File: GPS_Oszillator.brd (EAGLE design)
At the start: 100 x 80 mm, 33 parts, among them IC1 74ACT04D, IC2 7805TV, X1 ST-SMB-V, X2 ST-SMB-V

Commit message: Add files via upload
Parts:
- removed JP1: to_PB6, pinhead:1X02
- moved C12 41.6 mm to (91.7, 10.8), turned to 0 degrees
- moved JP6 6.40 mm to (25.8, 50.4), turned to 0 degrees
- moved C13 4.50 mm to (30.8, 54.8), turned to 90 degrees
- moved R4 3.05 mm to (20.7, 49.4), turned to 0 degrees
- moved IC1 0.45 mm to (19.4, 39.7)
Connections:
- removed net N$1: IC1.2, R3.2
- removed net RESET: U$2.P$4
- new net PPS_IN: IC1.2, R3.2, U$4.34
- new net PWM_OUT: IC1.11, U$4.32
- new net RST: U$2.P$4, U$4.17
- net 10MHZ_IN: now also U$4.35; no longer JP1.1
- net DC: now also U$4.16
- net GND: no longer IC1.11, JP1.2
- net PWM_16BIT: now also IC1.10
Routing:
- net RESET: track 73.5 -> 0.00 mm
- net 5V0: track 114.4 -> 179.6 mm
- net 3V3: track 45.2 -> 101.7 mm, vias 0 -> 2
- net DC: track 74.2 -> 33.3 mm, vias 0 -> 2
- net CS: track 71.8 -> 33.3 mm
- net RST: track 0.00 -> 33.4 mm, vias 0 -> 2
- net PPS_IN: track 0.00 -> 24.4 mm, vias 0 -> 1
- net PWM_OUT: track 0.00 -> 21.3 mm, vias 0 -> 2
- net N$1: track 20.2 -> 0.00 mm, vias 2 -> 0
- net ESP32_EN: track 0.00 -> 8.07 mm
- net 10MHZ_IN: track 38.1 -> 45.0 mm, vias 0 -> 1
- net MOSI: track 55.2 -> 61.3 mm
- net N$4: track 0.00 -> 6.04 mm
- net SCK: track 40.6 -> 46.0 mm, vias 0 -> 2
- net PWM_16BIT: track 17.7 -> 22.1 mm, vias 0 -> 2
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
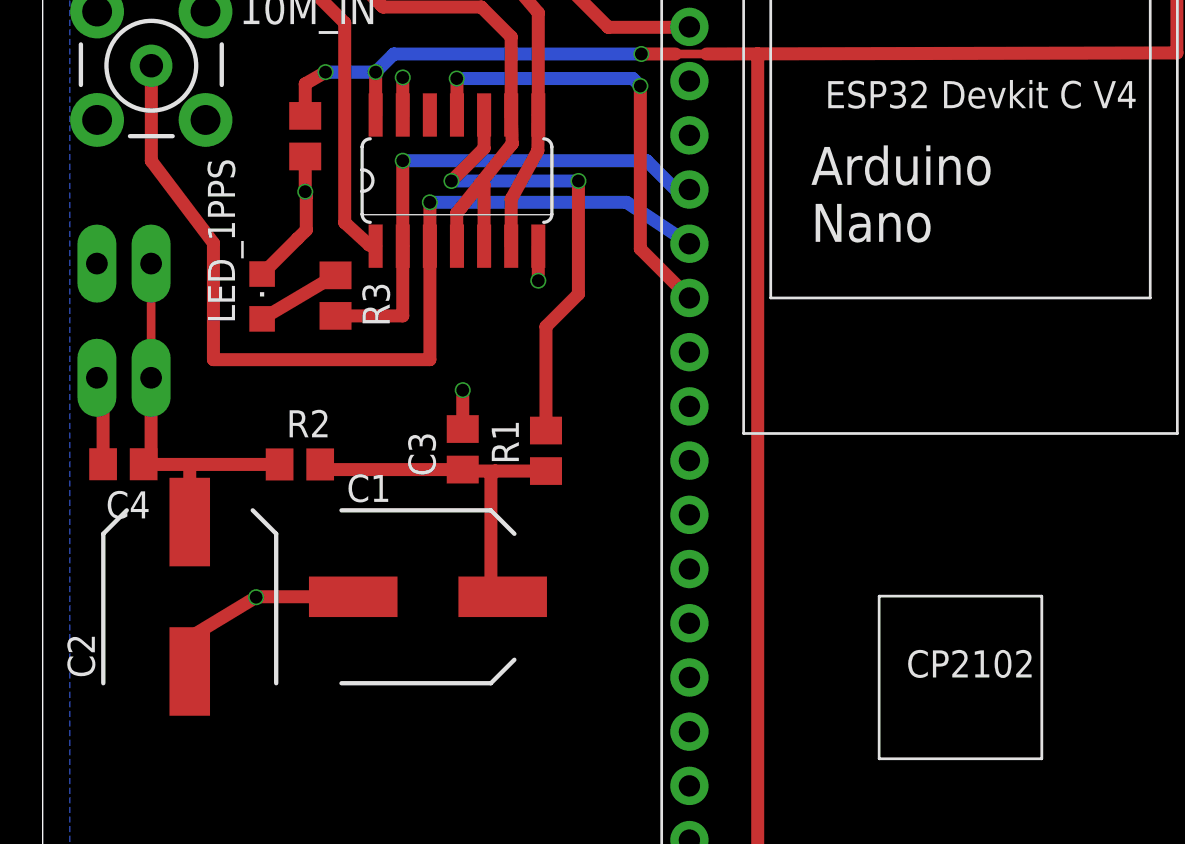
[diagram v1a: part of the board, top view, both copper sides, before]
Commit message: Change PWM filter
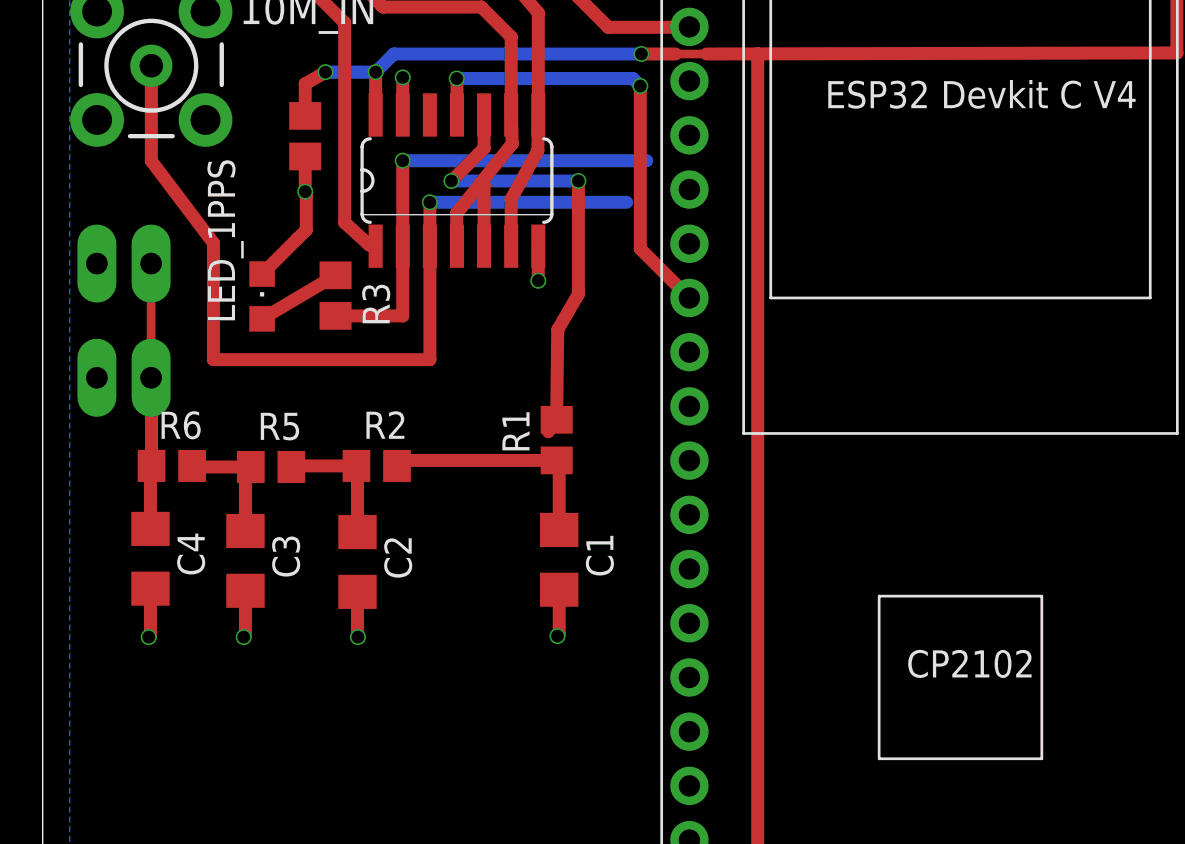
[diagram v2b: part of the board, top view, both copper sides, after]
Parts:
- added R5, R6: 1k, rcl:R0805
- C1: value 100µ -> 10µ; device rcl:SANYO-OSCON_SMD_E7 -> rcl:C1206
- C2: value nc -> 10µ; device rcl:SANYO-OSCON_SMD_E7 -> rcl:C1206
- C3: value 100n -> 10µ; device rcl:C0805 -> rcl:C1206
- C4: value nc -> 10µ; device rcl:C0805 -> rcl:C1206
- R1: value 10k -> 1k
- R2: value 0 -> 1k
- moved C3 11.4 mm to (9.50, 21.9), turned to 270 degrees
- moved C2 8.03 mm to (14.8, 21.9), turned to 270 degrees
- moved C1 6.39 mm to (24.2, 21.9), turned to 270 degrees
- moved C4 4.61 mm to (5.05, 22.0), turned to 270 degrees
- moved R2 3.60 mm to (15.7, 26.4)
- moved R1 0.71 mm to (24.1, 27.6)
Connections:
- new net N$1: C3.1, R5.1, R6.2
- new net N$3: C2.1, R2.1, R5.2
- net 10MHZ_IN: now also U$4.34; no longer U$4.35
- net GND: now also C1.2, C2.2; no longer C1.-, C2.-
- net N$5: now also C1.1; no longer C1.+, C3.1
- net N$6: now also R6.1; no longer C2.+, R2.1
- net PPS_IN: now also U$4.35; no longer U$4.34
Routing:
- net N$6: track 19.1 -> 12.5 mm
- net GND: track 59.0 -> 52.5 mm, vias 9 -> 11
- net N$3: track 0.00 -> 6.19 mm
- net N$5: track 16.9 -> 10.9 mm
- net N$1: track 0.00 -> 5.87 mm
- net 10MHZ_IN: track 45.0 -> 41.5 mm
- net PPS_IN: track 24.4 -> 21.8 mm
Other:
- board text removed: "Arduino Nano"

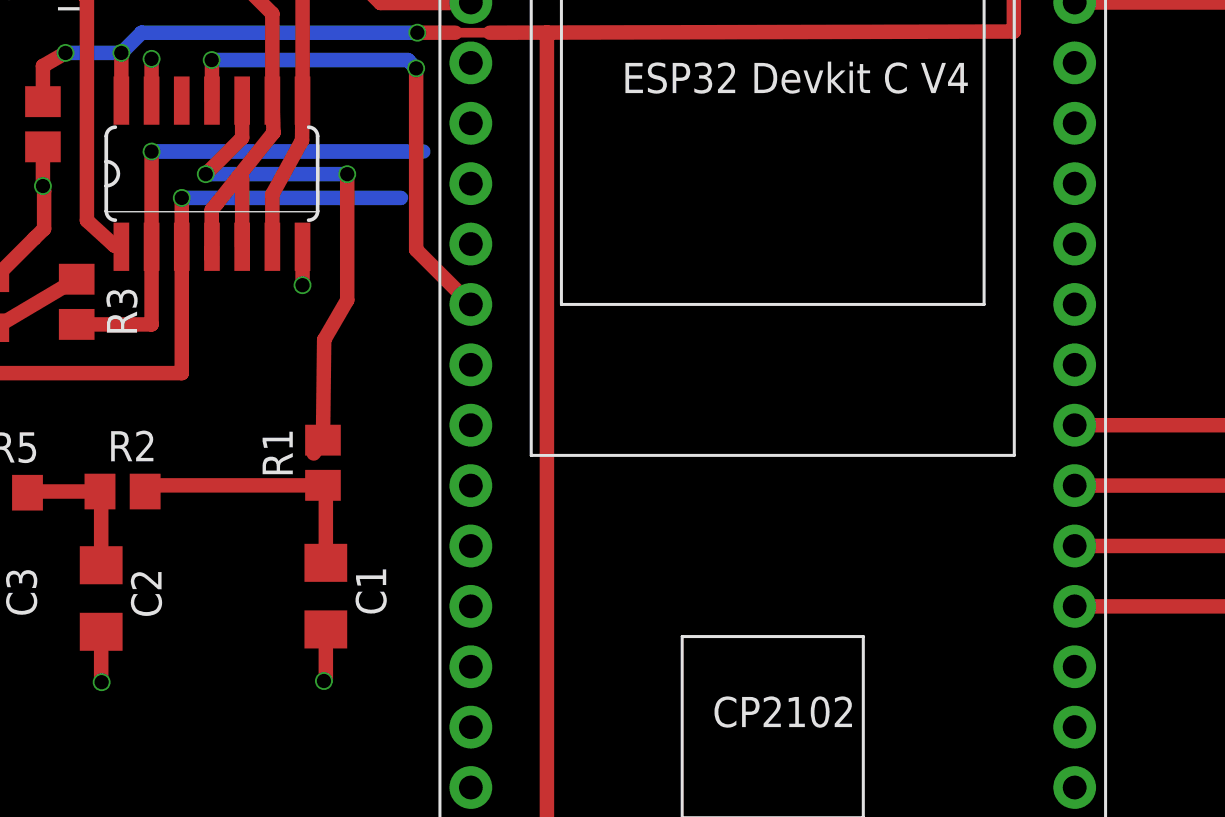
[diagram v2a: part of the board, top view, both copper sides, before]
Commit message: update esp32 inputs.
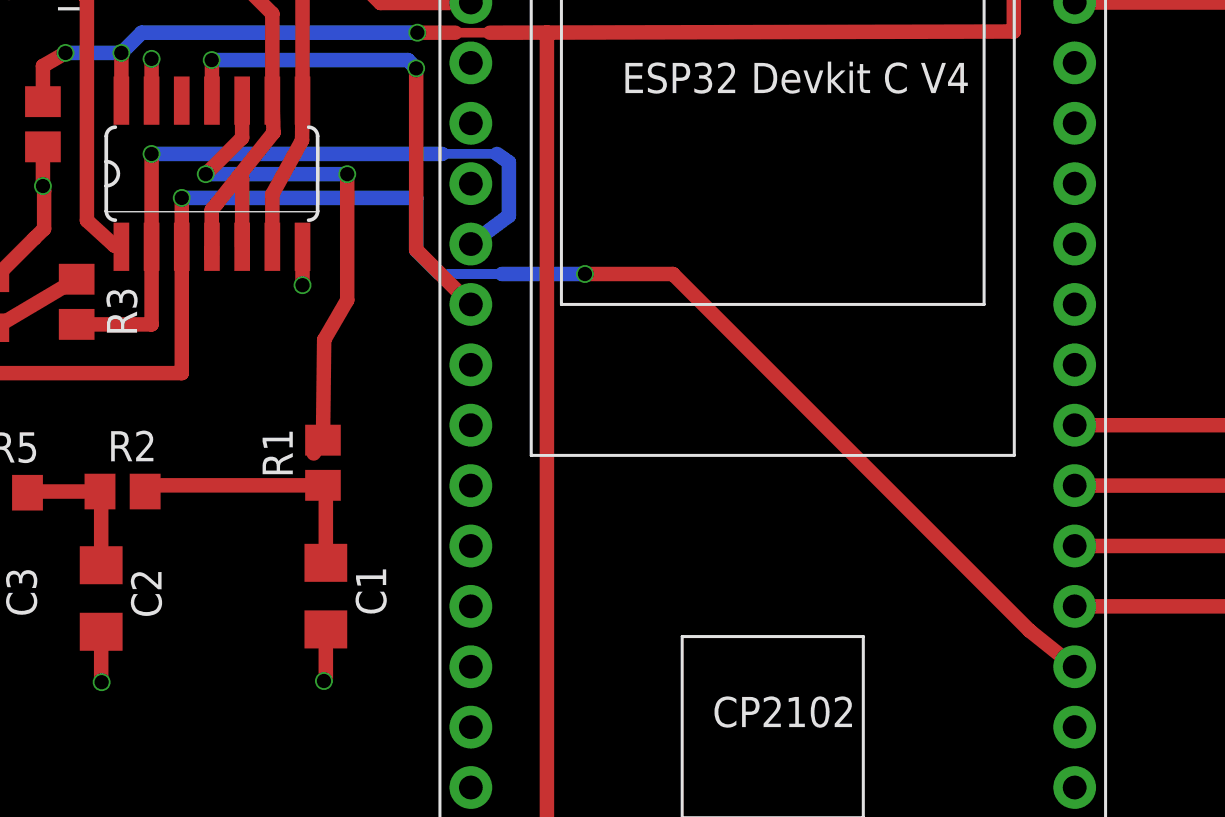
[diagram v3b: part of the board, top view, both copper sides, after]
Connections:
- net 10MHZ_IN: now also U$4.4; no longer U$4.34
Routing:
- net 10MHZ_IN: track 41.5 -> 79.2 mm, vias 1 -> 2
- net PPS_IN: track 21.8 -> 29.7 mm
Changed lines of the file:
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@@
 <wire x1="92.6" y1="10.75" x2="92.6" y2="10.7" width="0.6096" layer="1"/>
 <wire x1="92.6" y1="10.7" x2="94.25" y2="10.7" width="0.6096" layer="1"/>
-<via x="94.25" y="10.7" extent="1-16" drill="0.6"/>
+<via x="94.25" y="10.7" extent="1-16" drill="0.6" shape="octagon"/>
 <wire x1="2.83" y1="30.19" x2="2.54" y2="30.48" width="0.6096" layer="1"/>
 <contactref element="U$3" pad="2"/>
 <contactref element="IC1" pad="13"/>
 <contactref element="D1" pad="A"/>
-<via x="16.87" y="44.55" extent="1-16" drill="0.6"/>
+<via x="16.87" y="44.55" extent="1-16" drill="0.6" shape="octagon"/>
 <wire x1="16.87" y1="44.55" x2="16.87" y2="42.7734" width="0.6096" layer="1"/>
 <contactref element="C13" pad="2"/>
@@
 <via x="9.42" y="18.33" extent="1-16" drill="0.6" shape="octagon"/>
 <via x="4.97" y="18.33" extent="1-16" drill="0.6" shape="octagon"/>
-<wire x1="16.87" y1="42.7734" x2="16.87" y2="42.7934" width="0" layer="19" extent="1-1"/>
 <wire x1="24.12" y1="18.38" x2="24.2" y2="18.46" width="0.6096" layer="1"/>
 <wire x1="24.2" y1="18.46" x2="24.2" y2="20.55" width="0.6096" layer="1"/>
@@
 <wire x1="4.97" y1="18.33" x2="5.05" y2="18.41" width="0.6096" layer="1"/>
 <wire x1="5.05" y1="18.41" x2="5.05" y2="20.6" width="0.6096" layer="1"/>
+<wire x1="16.87" y1="42.7734" x2="16.87" y2="42.7934" width="0" layer="19" extent="1-1"/>
 </signal>
 <signal name="PPS_IN">
@@
 <wire x1="16.87" y1="36.6466" x2="16.87" y2="33.38" width="0.6096" layer="1"/>
 <wire x1="16.87" y1="33.38" x2="13.72" y2="33.38" width="0.6096" layer="1"/>
-<via x="16.87" y="40.65" extent="1-16" drill="0.6" shape="octagon"/>
-<wire x1="16.87" y1="40.65" x2="16.87" y2="36.6466" width="0.6096" layer="1"/>
-<wire x1="16.87" y1="40.65" x2="28.3" y2="40.65" width="0.6096" layer="16"/>
+<via x="16.87" y="40.55" extent="1-16" drill="0.6" shape="octagon"/>
+<wire x1="16.87" y1="40.55" x2="16.87" y2="36.6466" width="0.6096" layer="1"/>
+<wire x1="16.87" y1="40.55" x2="29.1" y2="40.55" width="0.6096" layer="16"/>
 <contactref element="U$4" pad="35"/>
-<wire x1="28.3" y1="40.65" x2="30.3" y2="36.76" width="0" layer="19" extent="16-16"/>
+<wire x1="29.1" y1="40.55" x2="31.4" y2="40.55" width="0.4064" layer="16"/>
+<wire x1="31.4" y1="40.55" x2="31.9" y2="40.2" width="0.6096" layer="16"/>
+<wire x1="31.9" y1="40.2" x2="31.9" y2="37.95" width="0.6096" layer="16"/>
+<wire x1="31.9" y1="37.95" x2="30.3" y2="36.76" width="0.6096" layer="16"/>
 </signal>
 <signal name="10MHZ_IN">
@@
 <wire x1="5.09" y1="40.64" x2="5.09" y2="45.1" width="0.6096" layer="1"/>
 <wire x1="18.14" y1="36.6466" x2="18.14" y2="38.7" width="0.6096" layer="1"/>
-<via x="18.14" y="38.7" extent="1-16" drill="0.6"/>
-<wire x1="18.14" y1="38.7" x2="27.36" y2="38.7" width="0.6096" layer="16"/>
-<contactref element="U$4" pad="34"/>
-<wire x1="27.36" y1="38.7" x2="30.3" y2="39.3" width="0" layer="19" extent="16-16"/>
+<via x="18.14" y="38.7" extent="1-16" drill="0.6" shape="octagon"/>
+<wire x1="18.14" y1="38.7" x2="28" y2="38.7" width="0.6096" layer="16"/>
+<contactref element="U$4" pad="4"/>
+<wire x1="55.7" y1="18.98" x2="53.8" y2="20.5" width="0.6096" layer="1"/>
+<wire x1="53.8" y1="20.5" x2="38.8" y2="35.5" width="0.6096" layer="1"/>
+<wire x1="38.8" y1="35.5" x2="35.1" y2="35.5" width="0.6096" layer="1"/>
+<wire x1="28" y1="38.7" x2="28" y2="36.5" width="0.6096" layer="16"/>
+<wire x1="28" y1="36.5" x2="29" y2="35.5" width="0.6096" layer="16"/>
+<wire x1="29" y1="35.5" x2="31.6" y2="35.5" width="0.4064" layer="16"/>
+<wire x1="31.6" y1="35.5" x2="35.1" y2="35.5" width="0.6096" layer="16"/>
+<via x="35.1" y="35.5" extent="1-16" drill="0.6" shape="octagon"/>
 </signal>
 <signal name="N$2">
@@
 <wire x1="72.61" y1="15.25" x2="70.45" y2="15.26" width="0.6096" layer="16"/>
 <wire x1="70.45" y1="15.26" x2="70.45" y2="27" width="0.6096" layer="16"/>
-<via x="70.45" y="27" extent="1-16" drill="0.6"/>
+<via x="70.45" y="27" extent="1-16" drill="0.6" shape="octagon"/>
 <contactref element="U$4" pad="5V"/>
 <wire x1="70.45" y1="27" x2="70.5" y2="53.7" width="0.6096" layer="1"/>
@@
 <wire x1="20.68" y1="42.7934" x2="20.68" y2="41.23" width="0.6096" layer="1"/>
 <wire x1="20.68" y1="41.23" x2="19.15" y2="39.7" width="0.6096" layer="1"/>
-<via x="19.15" y="39.7" extent="1-16" drill="0.6"/>
+<via x="19.15" y="39.7" extent="1-16" drill="0.6" shape="octagon"/>
 <wire x1="19.15" y1="39.7" x2="25.1" y2="39.7" width="0.6096" layer="16"/>
 <wire x1="25.1" y1="39.7" x2="25.1" y2="34.4" width="0.6096" layer="1"/>
 <wire x1="25.1" y1="34.4" x2="24.13" y2="32.73" width="0.6096" layer="1"/>
 <wire x1="24.13" y1="32.73" x2="24.08" y2="28.51" width="0.6096" layer="1"/>
-<via x="25.1" y="39.7" extent="1-16" drill="0.6"/>
+<via x="25.1" y="39.7" extent="1-16" drill="0.6" shape="octagon"/>
 </signal>
 <signal name="N$5">
@@
 <wire x1="66.7" y1="22.8" x2="66.7" y2="29.14" width="0.6096" layer="1"/>
 <wire x1="66.7" y1="29.14" x2="55.7" y2="29.14" width="0.6096" layer="1"/>
-<via x="87.85" y="22.8" extent="1-16" drill="0.6"/>
+<via x="87.85" y="22.8" extent="1-16" drill="0.6" shape="octagon"/>
 <wire x1="87.85" y1="22.8" x2="83.25" y2="22.8" width="0.6096" layer="16"/>
-<via x="83.25" y="22.8" extent="1-16" drill="0.6"/>
+<via x="83.25" y="22.8" extent="1-16" drill="0.6" shape="octagon"/>
 <wire x1="83.25" y1="22.8" x2="66.7" y2="22.8" width="0.6096" layer="1"/>
 </signal>
@@
 <wire x1="64.25" y1="24.06" x2="64.25" y2="20.3" width="0.6096" layer="1"/>
 <wire x1="64.25" y1="20.3" x2="75.55" y2="20.3" width="0.6096" layer="1"/>
-<via x="75.55" y="20.3" extent="1-16" drill="0.6"/>
+<via x="75.55" y="20.3" extent="1-16" drill="0.6" shape="octagon"/>
 <wire x1="75.55" y1="20.3" x2="80.25" y2="20.3" width="0.6096" layer="16"/>
-<via x="80.25" y="20.3" extent="1-16" drill="0.6"/>
+<via x="80.25" y="20.3" extent="1-16" drill="0.6" shape="octagon"/>
 <wire x1="80.25" y1="20.3" x2="80.23" y2="20.3" width="0.6096" layer="1"/>
 <wire x1="80.23" y1="20.3" x2="80.23" y2="15.25" width="0.6096" layer="1"/>
@@
 <wire x1="63.35" y1="18.8" x2="75.5" y2="18.8" width="0.6096" layer="1"/>
 <wire x1="75.5" y1="18.8" x2="75.5" y2="18.75" width="0.6096" layer="1"/>
-<via x="75.5" y="18.75" extent="1-16" drill="0.6"/>
+<via x="75.5" y="18.75" extent="1-16" drill="0.6" shape="octagon"/>
 <wire x1="75.5" y1="18.75" x2="82.75" y2="18.75" width="0.6096" layer="16"/>
 <wire x1="82.75" y1="18.75" x2="82.75" y2="18.7" width="0.6096" layer="16"/>
-<via x="82.75" y="18.7" extent="1-16" drill="0.6"/>
+<via x="82.75" y="18.7" extent="1-16" drill="0.6" shape="octagon"/>
 <wire x1="82.75" y1="18.7" x2="82.77" y2="18.7" width="0.6096" layer="1"/>
 <wire x1="82.77" y1="18.7" x2="82.77" y2="15.25" width="0.6096" layer="1"/>
@@
 <wire x1="19.41" y1="42.7934" x2="19.41" y2="44.49" width="0.6096" layer="1"/>
 <wire x1="19.41" y1="44.49" x2="19.4" y2="44.5" width="0.6096" layer="1"/>
-<via x="19.4" y="44.5" extent="1-16" drill="0.6"/>
+<via x="19.4" y="44.5" extent="1-16" drill="0.6" shape="octagon"/>
 <wire x1="19.4" y1="44.5" x2="27.65" y2="44.5" width="0.6096" layer="16"/>
 <wire x1="27.65" y1="44.5" x2="28" y2="44.15" width="0.6096" layer="16"/>
-<via x="28" y="44.15" extent="1-16" drill="0.6"/>
+<via x="28" y="44.15" extent="1-16" drill="0.6" shape="octagon"/>
 <wire x1="28" y1="44.15" x2="28" y2="36.52" width="0.6096" layer="1"/>
 <wire x1="28" y1="36.52" x2="30.3" y2="34.22" width="0.6096" layer="1"/>
